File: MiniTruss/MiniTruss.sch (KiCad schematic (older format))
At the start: 89 parts, among them IC1 HX711, IC2 HX711, IC3 HX711, IC4 HX711, IC5 HX711, IC6 HX711, IC7 HX711, IC8 HX711, J1 Conn_01x04_Male, J2 Conn_01x04_Male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

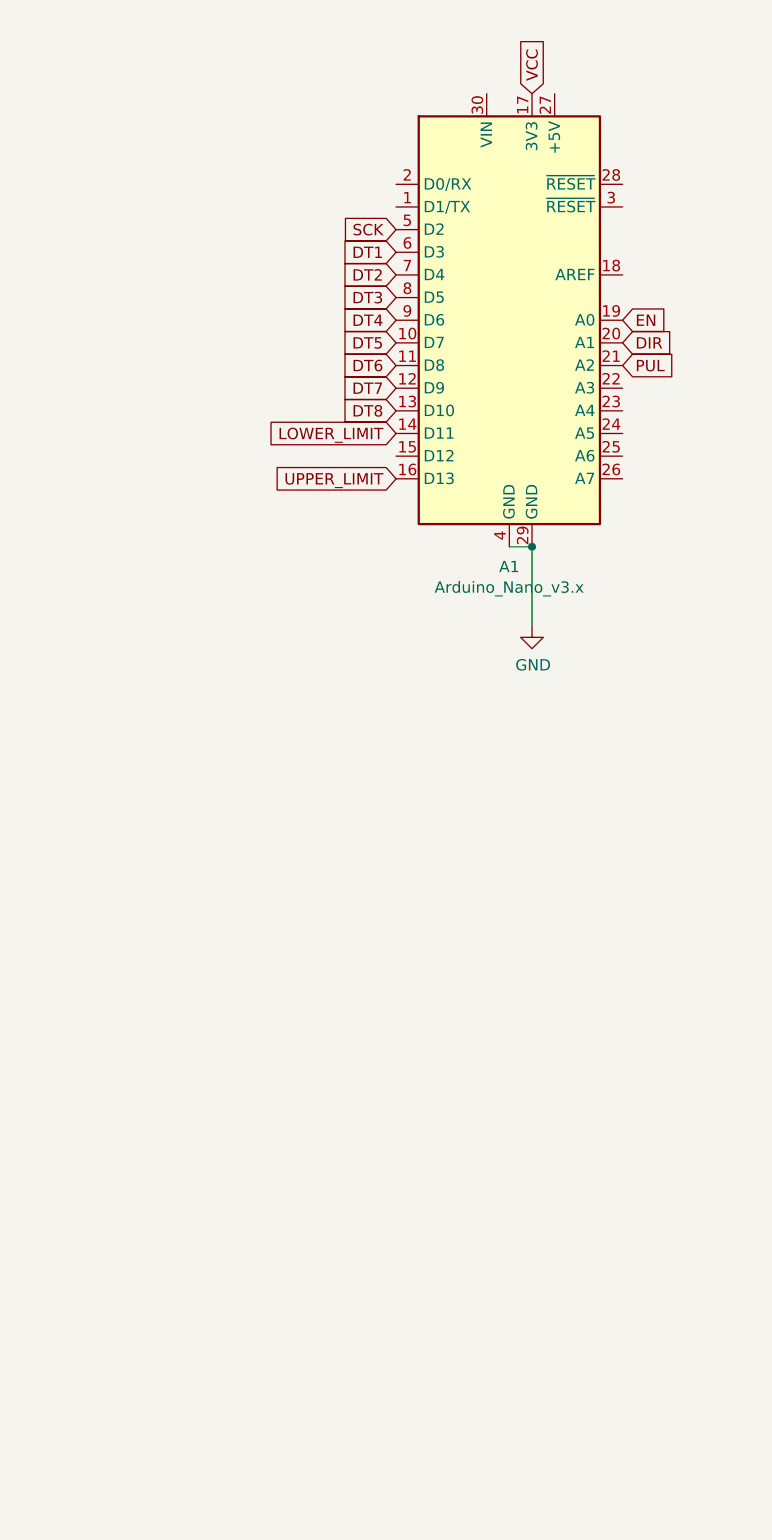
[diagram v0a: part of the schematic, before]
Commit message: added logic level shifter for linear actuator drive
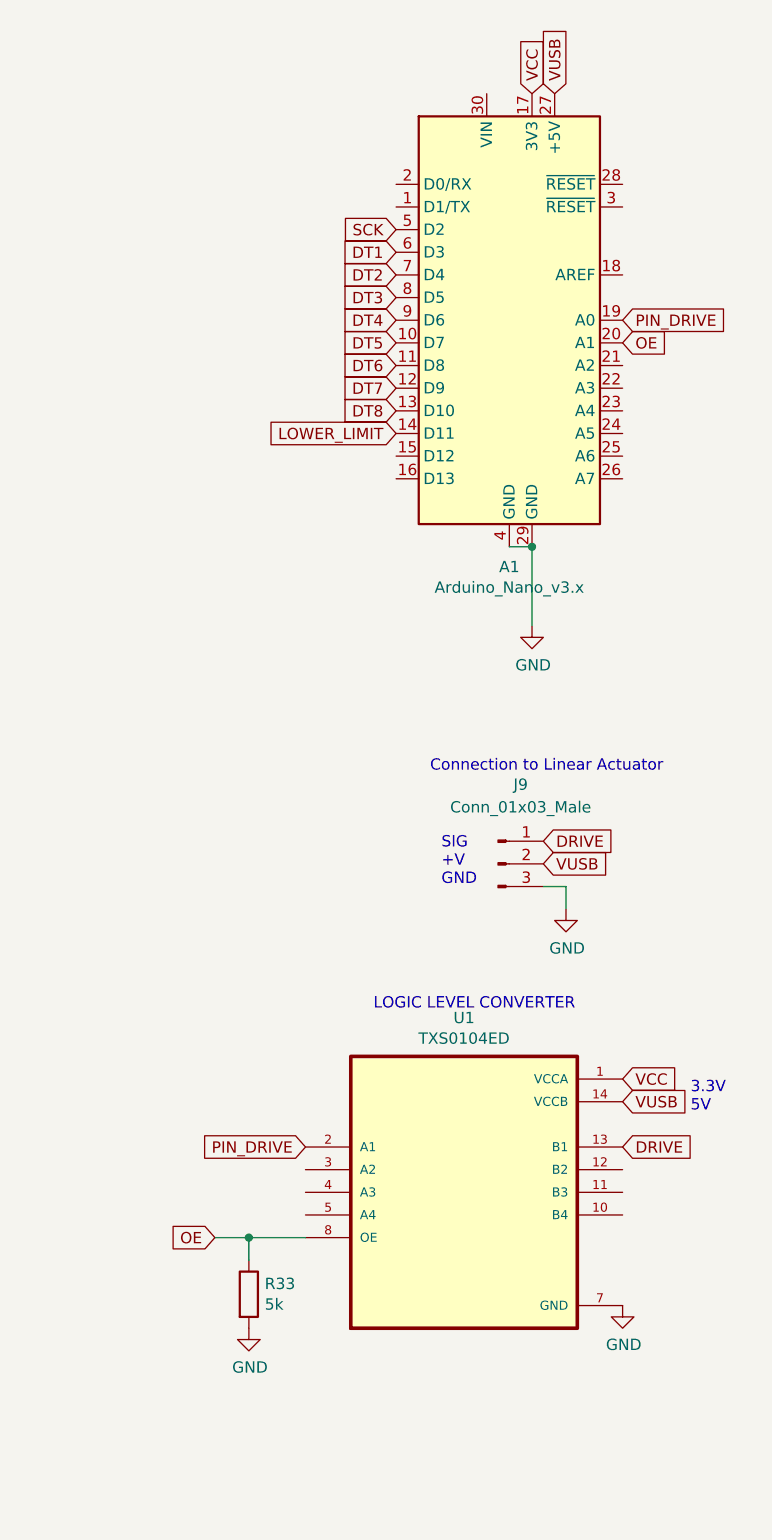
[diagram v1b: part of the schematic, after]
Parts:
- added J9: Conn_01x03_Male, symbol Connector:Conn_01x03_Male
- added R33: 5k, symbol Device:R
- added U1: TXS0104ED, SOIC127P600X175-14N, symbol TXS0104ED:TXS0104ED
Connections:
- net GND: now also J9.3 (Pin_3), R33.2, U1.7 (GND)
- net VCC: now also U1.1 (VCCA)
- net VUSB: now reaches A1.27 (+5V)
- net VUSB: now also J9.2 (Pin_2), U1.14 (VCCB)
- net DIR renamed OE
- net OE: now also R33.1, U1.8 (OE)
- net EN renamed PIN_DRIVE
- net PIN_DRIVE: now also U1.2 (A1)
- net PUL: no longer names the net of A1.21 (A2)
- net UPPER_LIMIT: no longer names the net of A1.16 (D13)
- new net DRIVE: J9.1 (Pin_1), U1.13 (B1)
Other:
- note added: "3.3V\n5V"
- note added: "Connection to Linear Actuator"
- note added: "LOGIC LEVEL CONVERTER"
- note added: "SIG\n+V\nGND"
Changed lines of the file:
@@
 Text GLabel 8750 1350 0    50   Input ~ 0
 SCK
-Text GLabel 9750 1750 2    50   Input ~ 0
-EN
-Text GLabel 9750 1850 2    50   Input ~ 0
-DIR
-Text GLabel 9750 1950 2    50   Input ~ 0
-PUL
-Text GLabel 8750 2450 0    50   Input ~ 0
-UPPER_LIMIT
+Text GLabel 9750 5400 2    50   Input ~ 0
+DRIVE
 Text GLabel 8750 2250 0    50   Input ~ 0
 LOWER_LIMIT
@@
 Text GLabel 9350 750  1    50   Input ~ 0
 VCC
+Text GLabel 9450 750  1    50   Input ~ 0
+VUSB
+$Comp
+L Connector:Conn_01x03_Male J9
+U 1 1 6295BCB2
+P 9200 4150
+F 0 "J9" H 9300 4500 50  0000 C CNN
+F 1 "Conn_01x03_Male" H 9300 4400 50  0000 C CNN
+F 2 "" H 9200 4150 50  0001 C CNN
+F 3 "~" H 9200 4150 50  0001 C CNN
+	1    9200 4150
+	1    0    0    -1
+$EndComp
+Text Notes 8900 3750 0    50   ~ 0
+Connection to Linear Actuator
+Text Notes 8950 4250 0    50   ~ 0
+SIG\n+V\nGND
+Text GLabel 9400 4050 2    50   Input ~ 0
+DRIVE
+Text GLabel 9400 4150 2    50   Input ~ 0
+VUSB
+$Comp
+L power:GND #PWR?
+U 1 1 6296FD6B
+P 9500 4350
+F 0 "#PWR?" H 9500 4100 50  0001 C CNN
+F 1 "GND" H 9505 4177 50  0000 C CNN
+F 2 "" H 9500 4350 50  0001 C CNN
+F 3 "" H 9500 4350 50  0001 C CNN
+	1    9500 4350
+	1    0    0    -1
+$EndComp
+Wire Wire Line
+	9400 4250 9500 4250
+Wire Wire Line
+	9500 4250 9500 4350
+$Comp
+L TXS0104ED:TXS0104ED U1
+U 1 1 629E0183
+P 9050 5600
+F 0 "U1" H 9050 6370 50  0000 C CNN
+F 1 "TXS0104ED" H 9050 6279 50  0000 C CNN
+F 2 "SOIC127P600X175-14N" H 9050 5600 50  0001 L BNN
+F 3 "" H 9050 5600 50  0001 L BNN
+	1    9050 5600
+	1    0    0    -1
+$EndComp
+$Comp
+L power:GND #PWR?
+U 1 1 629ED189
+P 9750 6100
+F 0 "#PWR?" H 9750 5850 50  0001 C CNN
+F 1 "GND" H 9755 5927 50  0000 C CNN
+F 2 "" H 9750 6100 50  0001 C CNN
+F 3 "" H 9750 6100 50  0001 C CNN
+	1    9750 6100
+	1    0    0    -1
+$EndComp
+Text GLabel 9750 5100 2    50   Input ~ 0
+VCC
+Text GLabel 9750 5200 2    50   Input ~ 0
+VUSB
+Text GLabel 7950 5800 0    50   Input ~ 0
+OE
+$Comp
+L Device:R R33
+U 1 1 62A2E1D6
+P 8100 6050
+F 0 "R33" H 8170 6096 50  0000 L CNN
+F 1 "5k" H 8170 6005 50  0000 L CNN
+F 2 "" V 8030 6050 50  0001 C CNN
+F 3 "~" H 8100 6050 50  0001 C CNN
+	1    8100 6050
+	1    0    0    -1
+$EndComp
+$Comp
+L power:GND #PWR?
+U 1 1 62A37819
+P 8100 6200
+F 0 "#PWR?" H 8100 5950 50  0001 C CNN
+F 1 "GND" H 8105 6027 50  0000 C CNN
+F 2 "" H 8100 6200 50  0001 C CNN
+F 3 "" H 8100 6200 50  0001 C CNN
+	1    8100 6200
+	1    0    0    -1
+$EndComp
+Wire Wire Line
+	7950 5800 8100 5800
+Wire Wire Line
+	8100 5900 8100 5800
+Connection ~ 8100 5800
+Wire Wire Line
+	8100 5800 8350 5800
+Text GLabel 9750 1850 2    50   Input ~ 0
+OE
+Text GLabel 9750 1750 2    50   Input ~ 0
+PIN_DRIVE
+Text GLabel 8350 5400 0    50   Input ~ 0
+PIN_DRIVE
+Text Notes 8650 4800 0    50   ~ 0
+LOGIC LEVEL CONVERTER
+Text Notes 10050 5250 0    50   ~ 0
+3.3V\n5V
 $EndSCHEMATC

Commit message: minor update to schematic
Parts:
- removed C29: 10uF, symbol Device:C
- removed C30: 10uF, symbol Device:C_Small
- removed C31, C32: 0.1uF, symbol Device:C_Small
- removed IC8: HX711, SOIC127P600X160-16N, symbol HX711:HX711
- removed J8: Conn_01x04_Male, symbol Connector:Conn_01x04_Male
- removed Q8: BC808, Package_TO_SOT_SMD:SOT-23, symbol Transistor_BJT:BC808
- removed R29, R31, R32: 100, symbol Device:R_Small
- removed R30: 150, symbol Device:R_Small
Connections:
- net PIN_DRIVE: now also A1.15 (D12); no longer A1.19 (A0)

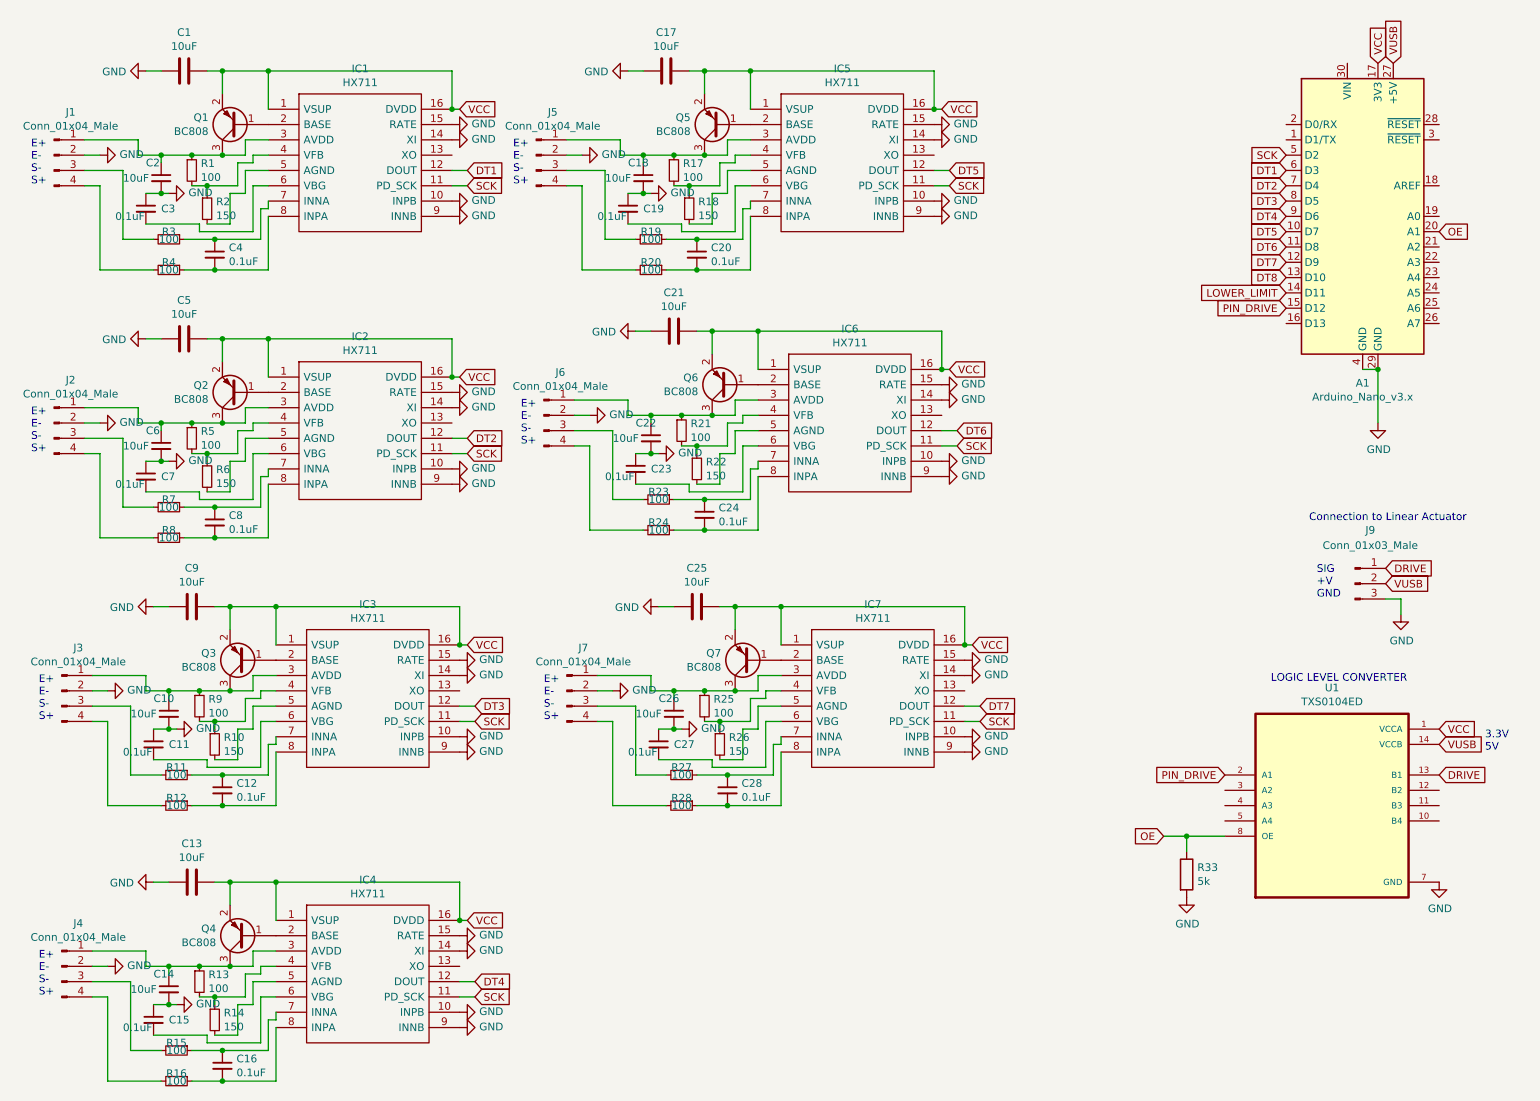
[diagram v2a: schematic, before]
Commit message: updated r1 and r2 values
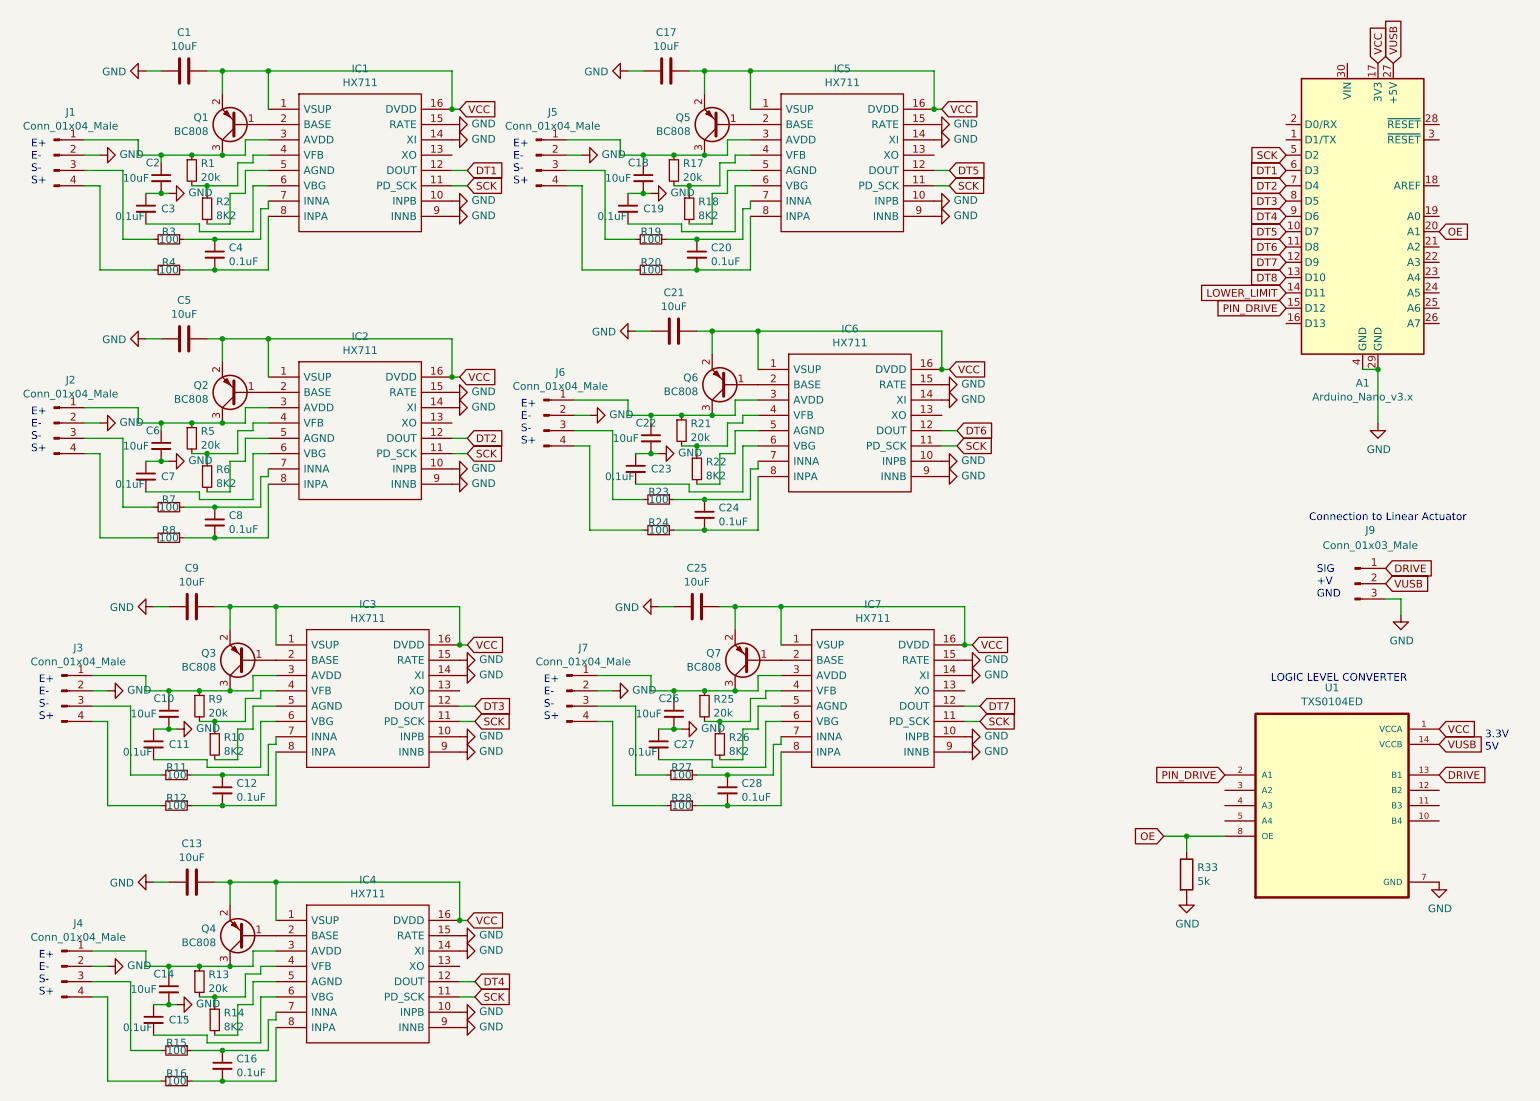
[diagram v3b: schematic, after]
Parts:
- R1, R13, R17, R21, R25, R5, R9: value 100 -> 20k
- R10, R14, R18, R2, R22, R26, R6: value 150 -> 8K2
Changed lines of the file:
@@
 P 1700 1700
 F 0 "R2" H 1759 1746 50  0000 L CNN
-F 1 "150" H 1759 1655 50  0000 L CNN
+F 1 "8K2" H 1759 1655 50  0000 L CNN
 F 2 "" H 1700 1700 50  0001 C CNN
 F 3 "~" H 1700 1700 50  0001 C CNN
@@
 P 1600 1450
 F 0 "R1" H 1659 1496 50  0000 L CNN
-F 1 "100" H 1659 1405 50  0000 L CNN
+F 1 "20k" H 1659 1405 50  0000 L CNN
 F 2 "" H 1600 1450 50  0001 C CNN
 F 3 "~" H 1600 1450 50  0001 C CNN
@@
 P 4850 1700
 F 0 "R18" H 4909 1746 50  0000 L CNN
-F 1 "150" H 4909 1655 50  0000 L CNN
+F 1 "8K2" H 4909 1655 50  0000 L CNN
 F 2 "" H 4850 1700 50  0001 C CNN
 F 3 "~" H 4850 1700 50  0001 C CNN
@@
 P 4750 1450
 F 0 "R17" H 4809 1496 50  0000 L CNN
-F 1 "100" H 4809 1405 50  0000 L CNN
+F 1 "20k" H 4809 1405 50  0000 L CNN
 F 2 "" H 4750 1450 50  0001 C CNN
 F 3 "~" H 4750 1450 50  0001 C CNN
@@
 P 4900 3400
 F 0 "R22" H 4959 3446 50  0000 L CNN
-F 1 "150" H 4959 3355 50  0000 L CNN
+F 1 "8K2" H 4959 3355 50  0000 L CNN
 F 2 "" H 4900 3400 50  0001 C CNN
 F 3 "~" H 4900 3400 50  0001 C CNN
@@
 P 4800 3150
 F 0 "R21" H 4859 3196 50  0000 L CNN
-F 1 "100" H 4859 3105 50  0000 L CNN
+F 1 "20k" H 4859 3105 50  0000 L CNN
 F 2 "" H 4800 3150 50  0001 C CNN
 F 3 "~" H 4800 3150 50  0001 C CNN
@@
 P 1700 3450
 F 0 "R6" H 1759 3496 50  0000 L CNN
-F 1 "150" H 1759 3405 50  0000 L CNN
+F 1 "8K2" H 1759 3405 50  0000 L CNN
 F 2 "" H 1700 3450 50  0001 C CNN
 F 3 "~" H 1700 3450 50  0001 C CNN
@@
 P 1600 3200
 F 0 "R5" H 1659 3246 50  0000 L CNN
-F 1 "100" H 1659 3155 50  0000 L CNN
+F 1 "20k" H 1659 3155 50  0000 L CNN
 F 2 "" H 1600 3200 50  0001 C CNN
 F 3 "~" H 1600 3200 50  0001 C CNN
@@
 P 1750 5200
 F 0 "R10" H 1809 5246 50  0000 L CNN
-F 1 "150" H 1809 5155 50  0000 L CNN
+F 1 "8K2" H 1809 5155 50  0000 L CNN
 F 2 "" H 1750 5200 50  0001 C CNN
 F 3 "~" H 1750 5200 50  0001 C CNN
@@
 P 1650 4950
 F 0 "R9" H 1709 4996 50  0000 L CNN
-F 1 "100" H 1709 4905 50  0000 L CNN
+F 1 "20k" H 1709 4905 50  0000 L CNN
 F 2 "" H 1650 4950 50  0001 C CNN
 F 3 "~" H 1650 4950 50  0001 C CNN
@@
 P 1750 7000
 F 0 "R14" H 1809 7046 50  0000 L CNN
-F 1 "150" H 1809 6955 50  0000 L CNN
+F 1 "8K2" H 1809 6955 50  0000 L CNN
 F 2 "" H 1750 7000 50  0001 C CNN
 F 3 "~" H 1750 7000 50  0001 C CNN
@@
 P 1650 6750
 F 0 "R13" H 1709 6796 50  0000 L CNN
-F 1 "100" H 1709 6705 50  0000 L CNN
+F 1 "20k" H 1709 6705 50  0000 L CNN
 F 2 "" H 1650 6750 50  0001 C CNN
 F 3 "~" H 1650 6750 50  0001 C CNN
@@
 P 5050 5200
 F 0 "R26" H 5109 5246 50  0000 L CNN
-F 1 "150" H 5109 5155 50  0000 L CNN
+F 1 "8K2" H 5109 5155 50  0000 L CNN
 F 2 "" H 5050 5200 50  0001 C CNN
 F 3 "~" H 5050 5200 50  0001 C CNN
@@
 P 4950 4950
 F 0 "R25" H 5009 4996 50  0000 L CNN
-F 1 "100" H 5009 4905 50  0000 L CNN
+F 1 "20k" H 5009 4905 50  0000 L CNN
 F 2 "" H 4950 4950 50  0001 C CNN
 F 3 "~" H 4950 4950 50  0001 C CNN
